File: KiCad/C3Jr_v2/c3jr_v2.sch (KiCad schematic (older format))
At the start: 35 parts, among them P43 CONN_1, Q17 2N5401, SW1 INC, SW2 DEC, SW3 MODE, SW4 RST, SW5 ENTER, U3 ATMEGA8-P, U4 74LS154, U5 STP8DP05, X1 16MHz

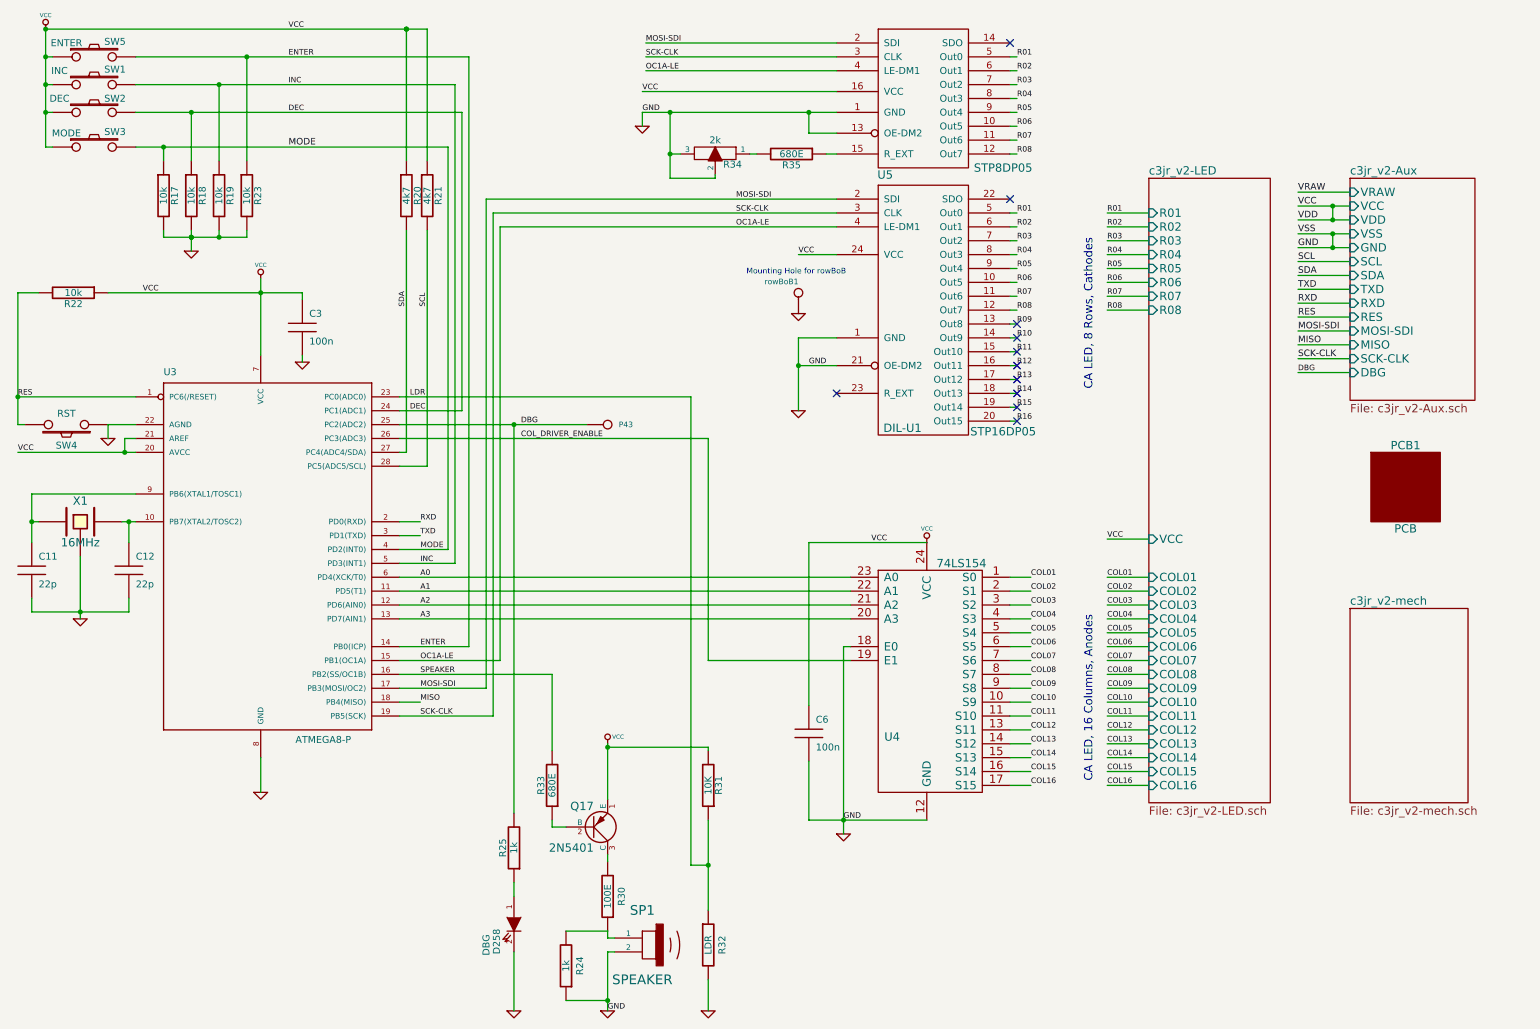
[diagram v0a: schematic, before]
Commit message: C3jr_v2-Added extra buttons for rear side. Some track clean up. Added OSHW and WyoLum Logos. Final for Production.
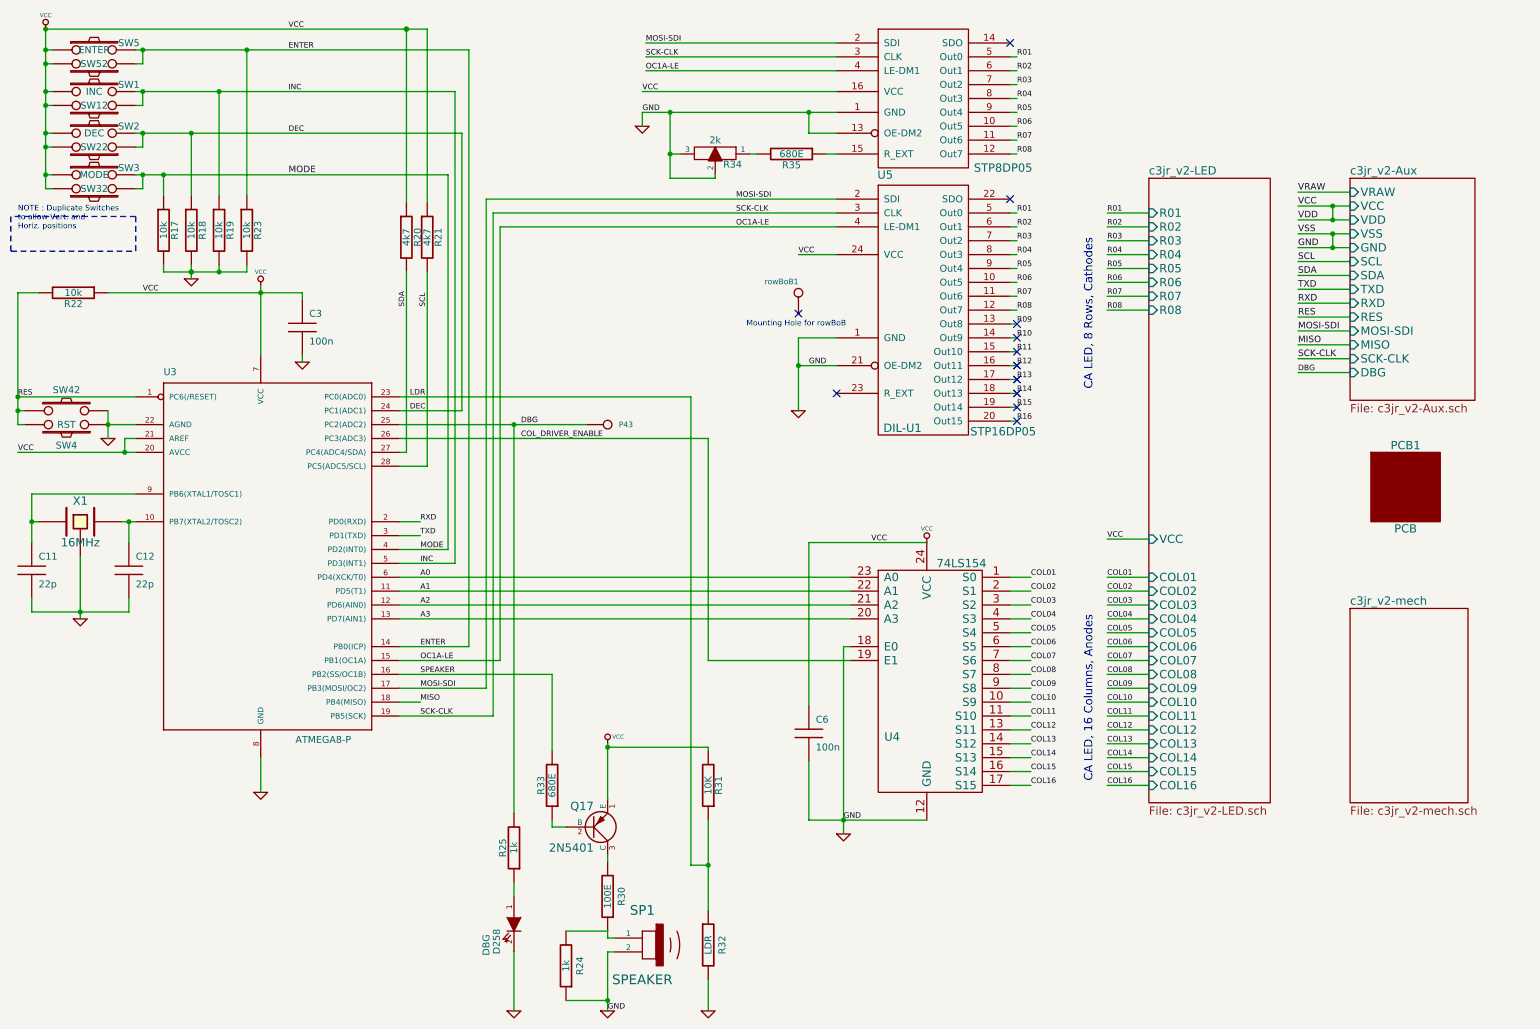
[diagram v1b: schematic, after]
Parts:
- added SW12: INC, SW-PB-MOD, symbol SW_PUSH
- added SW22: DEC, SW-PB-MOD, symbol SW_PUSH
- added SW32: MODE, SW-PB-MOD, symbol SW_PUSH
- added SW42: RST, SW-PB-MOD, symbol SW_PUSH
- added SW52: ENTER, SW-PB-MOD, symbol SW_PUSH
- PCB1: footprint (none) -> PCB
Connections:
- net DEC: now also SW22.1
- net ENTER: now also SW52.1
- net GND: now also SW42.2; no longer rowBoB1.1
- net INC: now also SW12.1
- net MODE: now also SW32.1
- net RES: now also SW42.1
- net VCC: now also SW12.2, SW22.2, SW32.2, SW52.2
- no-connect marks 11 -> 12
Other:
- note added: "NOTE : Duplicate Switches\nto allow Vert. and \nHoriz. positions"
- moved on the sheet: R17, R18, R19, R20, R21, R23, SW1, SW2, SW3, SW5

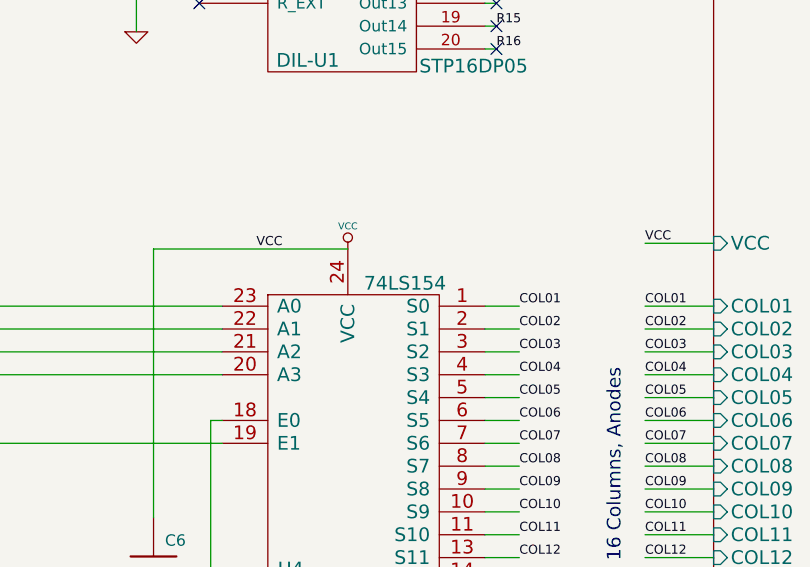
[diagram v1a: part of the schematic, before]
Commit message: C3Jr_v2 Connected Chronodot pins, added OpenHW and WyoLum logos, etc
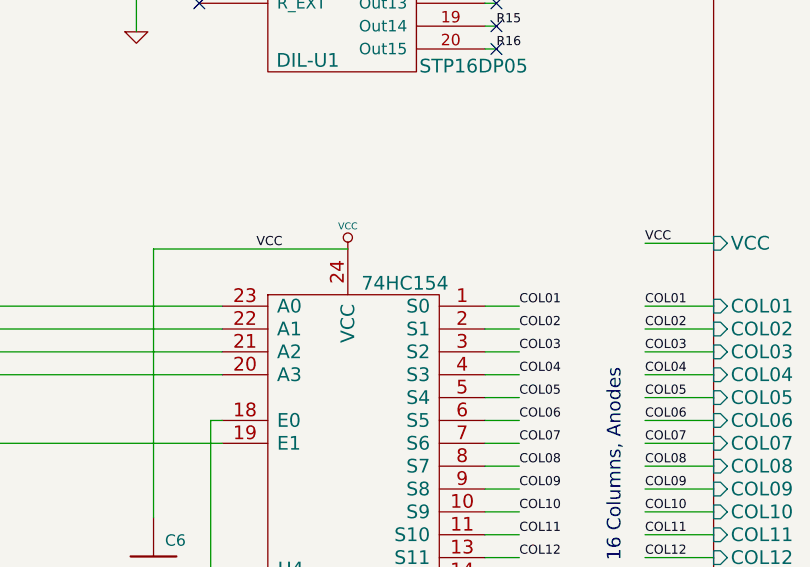
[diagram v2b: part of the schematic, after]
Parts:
- U4: value 74LS154 -> 74HC154
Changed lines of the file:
@@
-EESchema Schematic File Version 2  date 1/5/2012 2:50:43 PM
+EESchema Schematic File Version 2  date 1/7/2012 2:53:50 PM
 LIBS:C3Jr_v2
 LIBS:power
@@
 Sheet 1 4
 Title "ClockTHREE Junior aka C3Jr_v2 , with stackable board"
-Date "4 jan 2012"
+Date "7 jan 2012"
 Rev "A"
 Comp "an improved WordClock based on ClockTHREE"
@@
 P 7150 5350
 F 0 "U4" H 6900 5000 60  0000 C CNN
-F 1 "74LS154" H 7400 6250 60  0000 C CNN
+F 1 "74HC154" H 7400 6250 60  0000 C CNN
 F 2 "DIP-24__600_ELL" H 7150 5350 60  0001 C CNN
 F 3 "http://media.digikey.com/pdf/Data%20Sheets/Texas%20Instruments%20PDFs/SN74154.pdf" H 7150 5350 60  0001 C CNN

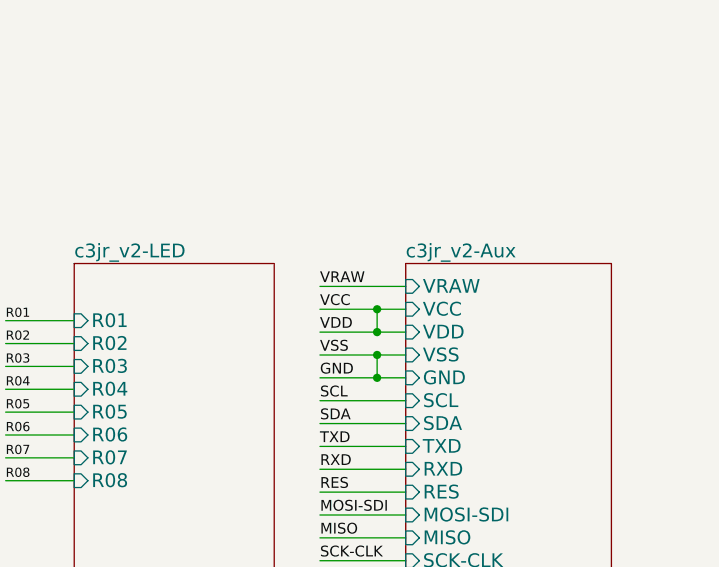
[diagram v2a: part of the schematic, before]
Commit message: c3jr_v2 user guide
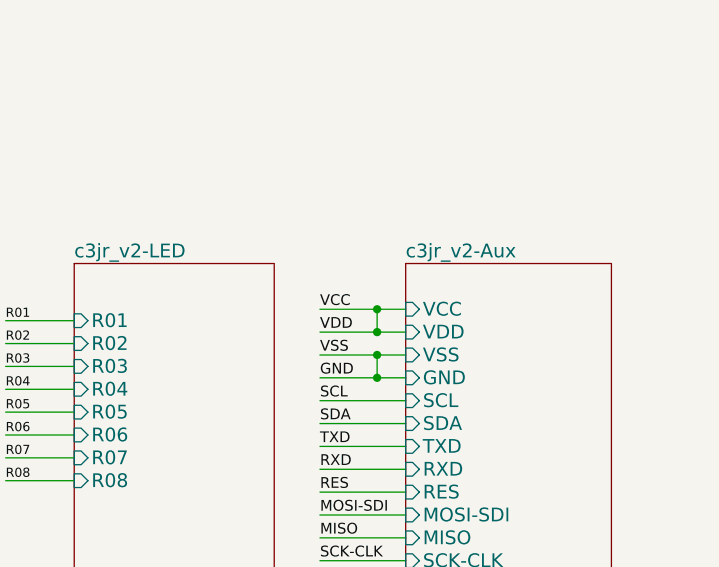
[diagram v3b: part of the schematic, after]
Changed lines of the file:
@@
-EESchema Schematic File Version 2  date 1/7/2012 2:53:50 PM
+EESchema Schematic File Version 2  date Sunday 22 January 2012 12:19:31 PM IST
 LIBS:C3Jr_v2
 LIBS:power
@@
 Sheet 1 4
 Title "ClockTHREE Junior aka C3Jr_v2 , with stackable board"
-Date "7 jan 2012"
+Date "22 jan 2012"
 Rev "A"
 Comp "an improved WordClock based on ClockTHREE"
@@
 Comment4 ""
 $EndDescr
+$Sheet
+S 10200 1675 900  1600
+U 4B3F1092
+F0 "c3jr_v2-Aux" 60
+F1 "c3jr_v2-Aux.sch" 60
+F2 "GND" I L 10200 2175 60
+F3 "VSS" I L 10200 2075 60
+F4 "SCL" I L 10200 2275 60
+F5 "SDA" I L 10200 2375 60
+F6 "MISO" I L 10200 2875 60
+F7 "RXD" I L 10200 2575 60
+F8 "TXD" I L 10200 2475 60
+F9 "RES" I L 10200 2675 60
+F10 "VDD" I L 10200 1975 60
+F11 "VCC" I L 10200 1875 60
+F12 "SCK-CLK" I L 10200 2975 60
+F13 "MOSI-SDI" I L 10200 2775 60
+F14 "DBG" I L 10200 3075 60
+$EndSheet
 Wire Notes Line
 	550  2200 550  1950
@@
 Wire Wire Line
 	4700 3450 3350 3450
-Wire Wire Line
-	9825 1775 10200 1775
 Wire Wire Line
 	10200 1975 9825 1975
@@
 Text Label 3550 2600 1    39   ~ 0
 SCL
-Text Label 9825 1775 0    47   ~ 0
-VRAW
 Text Label 9825 2075 0    47   ~ 0
 VSS
@@
 Text Label 3500 4150 0    39   ~ 0
 RXD
-$Sheet
-S 10200 1675 900  1600
-U 4B3F1092
-F0 "c3jr_v2-Aux" 60
-F1 "c3jr_v2-Aux.sch" 60
-F2 "GND" I L 10200 2175 60
-F3 "VSS" I L 10200 2075 60
-F4 "SCL" I L 10200 2275 60
-F5 "SDA" I L 10200 2375 60
-F6 "MISO" I L 10200 2875 60
-F7 "RXD" I L 10200 2575 60
-F8 "TXD" I L 10200 2475 60
-F9 "RES" I L 10200 2675 60
-F10 "VDD" I L 10200 1975 60
-F11 "VCC" I L 10200 1875 60
-F12 "VRAW" I L 10200 1775 60
-F13 "SCK-CLK" I L 10200 2975 60
-F14 "MOSI-SDI" I L 10200 2775 60
-F15 "DBG" I L 10200 3075 60
-$EndSheet
 Text Label 2550 1050 0    39   ~ 0
 INC

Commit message: C3Jr_v2 Switches moved 0.6" to left (for i2sd). Added C1 and C2 (100uF) for C3SB filtering
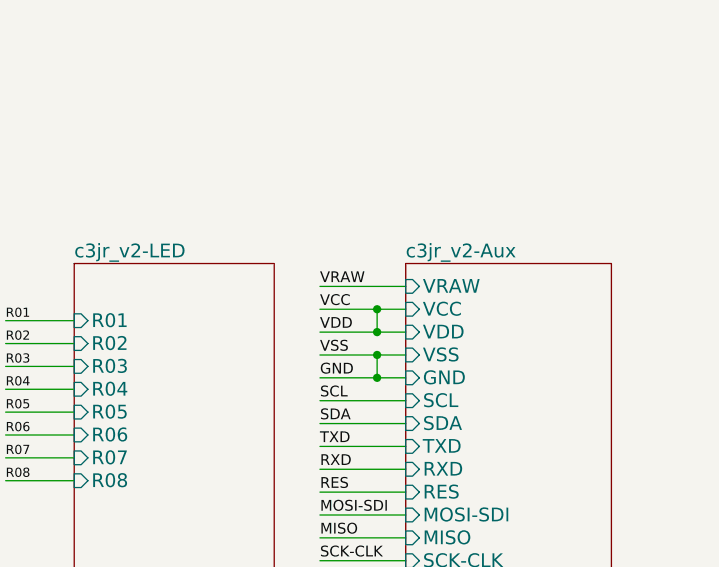
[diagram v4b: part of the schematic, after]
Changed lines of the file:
@@
-EESchema Schematic File Version 2  date Sunday 22 January 2012 12:19:31 PM IST
+EESchema Schematic File Version 2  date 1/23/2012 5:52:41 PM
 LIBS:C3Jr_v2
 LIBS:power
@@
 Sheet 1 4
 Title "ClockTHREE Junior aka C3Jr_v2 , with stackable board"
-Date "22 jan 2012"
+Date "23 jan 2012"
 Rev "A"
 Comp "an improved WordClock based on ClockTHREE"
@@
 Comment4 ""
 $EndDescr
-$Sheet
-S 10200 1675 900  1600
-U 4B3F1092
-F0 "c3jr_v2-Aux" 60
-F1 "c3jr_v2-Aux.sch" 60
-F2 "GND" I L 10200 2175 60
-F3 "VSS" I L 10200 2075 60
-F4 "SCL" I L 10200 2275 60
-F5 "SDA" I L 10200 2375 60
-F6 "MISO" I L 10200 2875 60
-F7 "RXD" I L 10200 2575 60
-F8 "TXD" I L 10200 2475 60
-F9 "RES" I L 10200 2675 60
-F10 "VDD" I L 10200 1975 60
-F11 "VCC" I L 10200 1875 60
-F12 "SCK-CLK" I L 10200 2975 60
-F13 "MOSI-SDI" I L 10200 2775 60
-F14 "DBG" I L 10200 3075 60
-$EndSheet
 Wire Notes Line
 	550  2200 550  1950
@@
 Wire Wire Line
 	4700 3450 3350 3450
+Wire Wire Line
+	9825 1775 10200 1775
 Wire Wire Line
 	10200 1975 9825 1975
@@
 Text Label 3550 2600 1    39   ~ 0
 SCL
+Text Label 9825 1775 0    47   ~ 0
+VRAW
 Text Label 9825 2075 0    47   ~ 0
 VSS
@@
 Text Label 3500 4150 0    39   ~ 0
 RXD
+$Sheet
+S 10200 1675 900  1600
+U 4B3F1092
+F0 "c3jr_v2-Aux" 60
+F1 "c3jr_v2-Aux.sch" 60
+F2 "GND" I L 10200 2175 60
+F3 "VSS" I L 10200 2075 60
+F4 "SCL" I L 10200 2275 60
+F5 "SDA" I L 10200 2375 60
+F6 "MISO" I L 10200 2875 60
+F7 "RXD" I L 10200 2575 60
+F8 "TXD" I L 10200 2475 60
+F9 "RES" I L 10200 2675 60
+F10 "VDD" I L 10200 1975 60
+F11 "VCC" I L 10200 1875 60
+F12 "VRAW" I L 10200 1775 60
+F13 "SCK-CLK" I L 10200 2975 60
+F14 "MOSI-SDI" I L 10200 2775 60
+F15 "DBG" I L 10200 3075 60
+$EndSheet
 Text Label 2550 1050 0    39   ~ 0
 INC

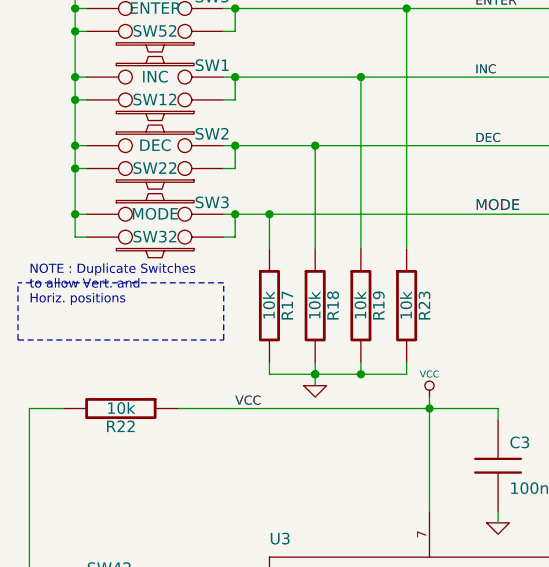
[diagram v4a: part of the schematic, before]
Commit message: C3jr_v2 : added jumper selector for RTC select, 2 pin headers for Switches, cleaned top Silk, Mini_USB error rectified. Gerber plots ready for a pre-production trial.
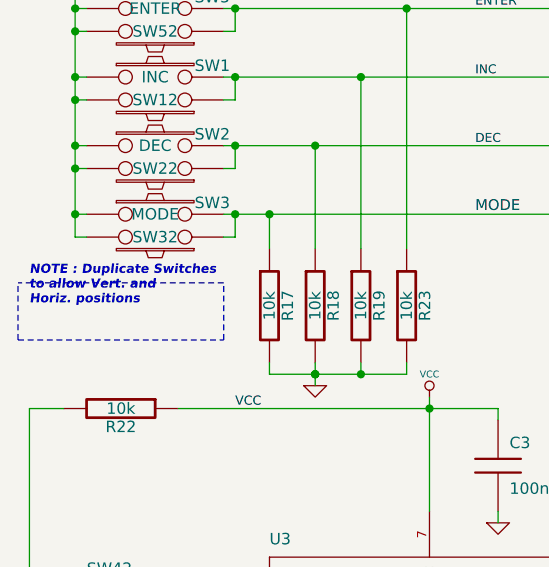
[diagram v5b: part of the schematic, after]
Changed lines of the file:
@@
-EESchema Schematic File Version 2  date 1/23/2012 5:52:41 PM
+EESchema Schematic File Version 2  date 2/11/2012 5:26:33 PM
 LIBS:C3Jr_v2
 LIBS:power
@@
 Sheet 1 4
 Title "ClockTHREE Junior aka C3Jr_v2 , with stackable board"
-Date "23 jan 2012"
+Date "11 feb 2012"
 Rev "A"
 Comp "an improved WordClock based on ClockTHREE"
@@
 	1500 1750 1500 1650
 Connection ~ 1500 1650
-Text Notes 600  2050 0    40   ~ 0
+Text Notes 600  2050 0    40   Italic 8
 NOTE : Duplicate Switches\nto allow Vert. and \nHoriz. positions
 $Comp

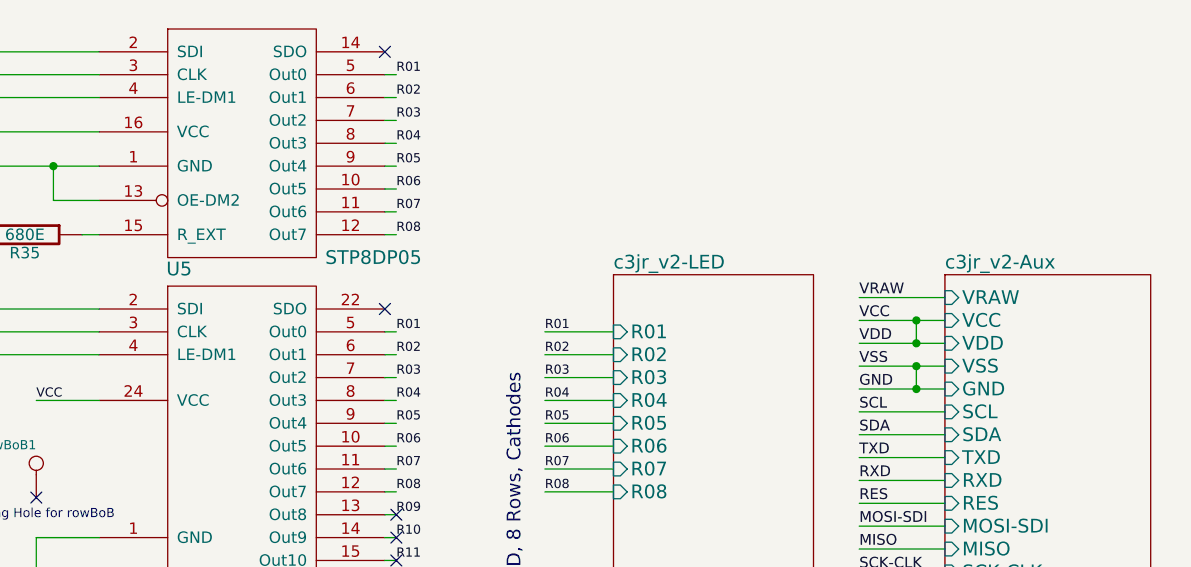
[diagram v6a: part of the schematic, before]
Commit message: C3jr_v2 : removed V_OUT (P12) header. Added 7805 Volt Reg (TO-220 horizontal) and 100nF Cap "C4" on output of V. Reg. Final Gerbers for trial boards from seeed.
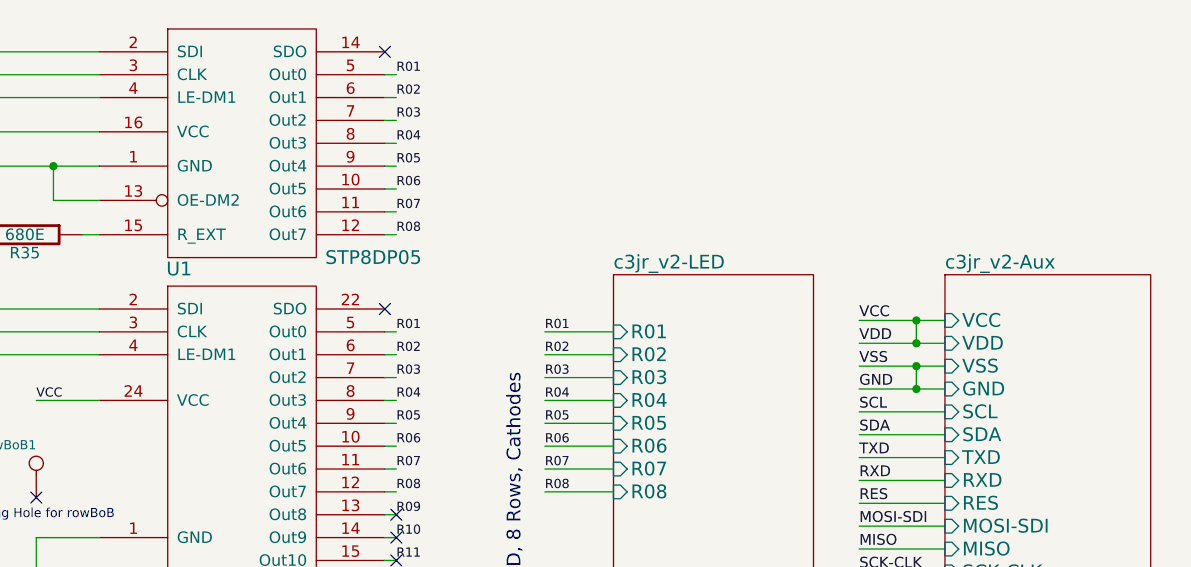
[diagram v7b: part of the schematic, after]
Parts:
- renumbered U5 to U1
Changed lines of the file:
@@
-EESchema Schematic File Version 2  date 2/13/2012 3:14:02 PM
+EESchema Schematic File Version 2  date 2/14/2012 6:32:43 PM
 LIBS:C3Jr_v2
 LIBS:power
@@
 Sheet 1 4
 Title "ClockTHREE Junior aka C3Jr_v2 , with stackable board"
-Date "13 feb 2012"
+Date "14 feb 2012"
 Rev "A"
 Comp "an improved WordClock based on ClockTHREE"
@@
 Wire Wire Line
 	4700 3450 3350 3450
-Wire Wire Line
-	9825 1775 10200 1775
 Wire Wire Line
 	10200 1975 9825 1975
@@
 NoConn ~ 7750 700
 $Comp
-L STP8DP05 U5
+L STP8DP05 U1
 U 1 1 4DB95F47
 P 7150 1500
-F 0 "U5" H 6850 1350 60  0000 C CNN
+F 0 "U1" H 6850 1350 60  0000 C CNN
 F 1 "STP8DP05" H 7700 1400 60  0000 C CNN
 F 2 "dil_16-300_socket" H 7150 1500 60  0001 C CNN
@@
 Text Label 3550 2600 1    39   ~ 0
 SCL
-Text Label 9825 1775 0    47   ~ 0
-VRAW
 Text Label 9825 2075 0    47   ~ 0
 VSS
@@
 F10 "VDD" I L 10200 1975 60
 F11 "VCC" I L 10200 1875 60
-F12 "VRAW" I L 10200 1775 60
-F13 "SCK-CLK" I L 10200 2975 60
-F14 "MOSI-SDI" I L 10200 2775 60
-F15 "DBG" I L 10200 3075 60
+F12 "SCK-CLK" I L 10200 2975 60
+F13 "MOSI-SDI" I L 10200 2775 60
+F14 "DBG" I L 10200 3075 60
 $EndSheet
 Text Label 2550 1050 0    39   ~ 0
